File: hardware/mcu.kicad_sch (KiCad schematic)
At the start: 35 parts, among them J10 Conn_01x06, J11 Conn_01x02, J7 TC2030, J8 Conn_01x04, J9 Conn_01x06, U3 AT25SF081-SSHD-B, U4 MCP9808, U5 STM32L552CEU6, Y1 ECS-160-9-37-CKM-TR3, Y2 ABS05-32.768KHZ-9-T

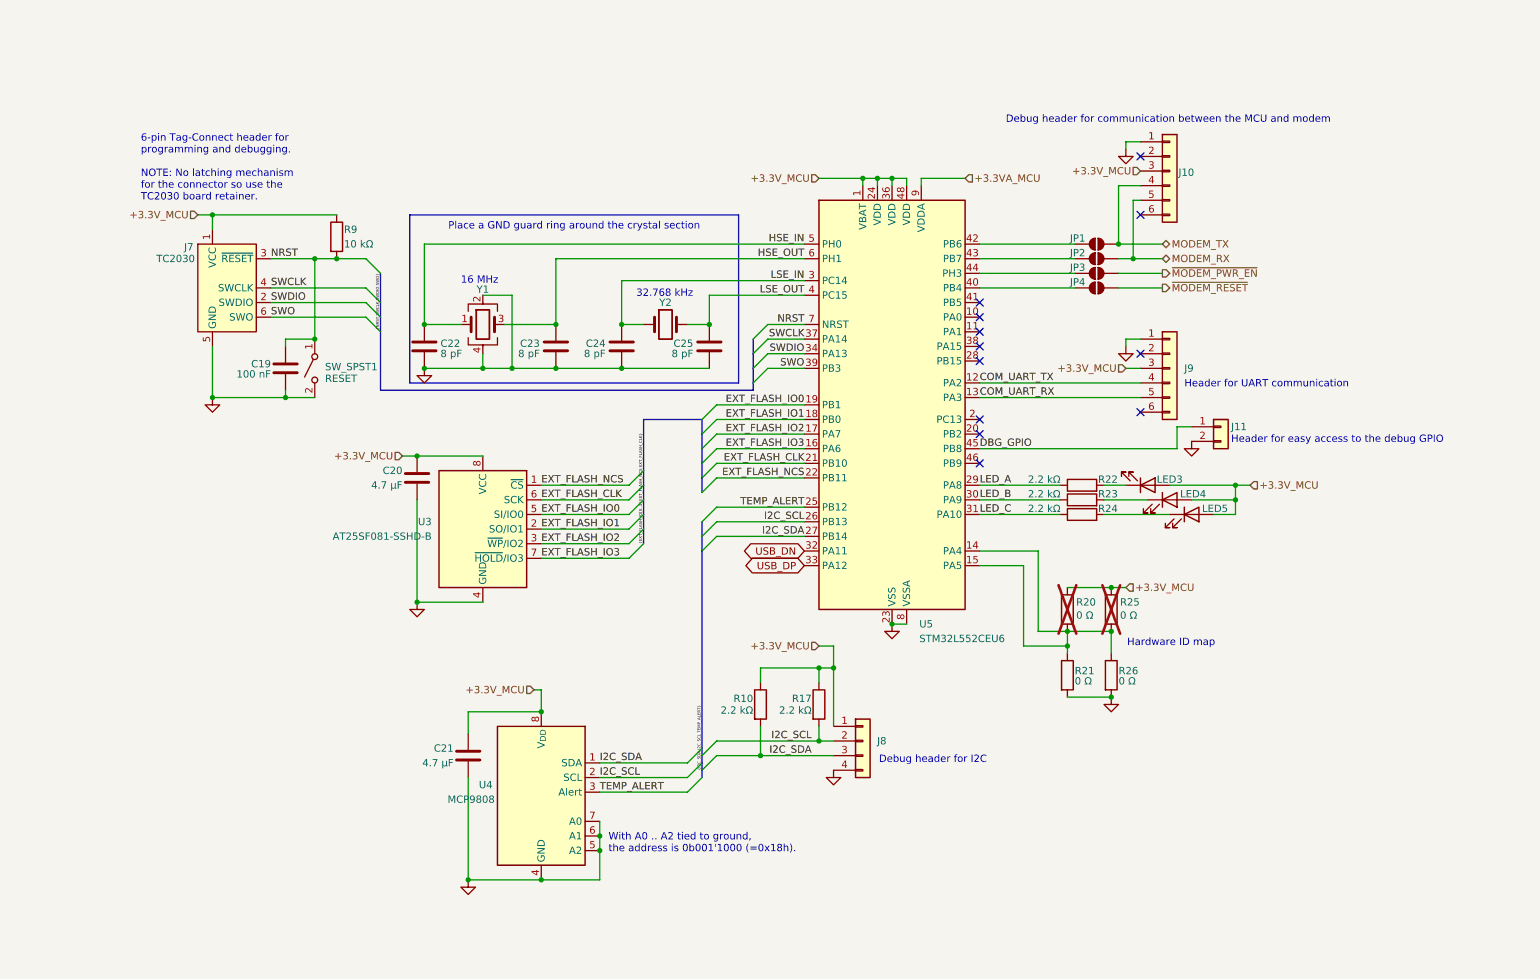
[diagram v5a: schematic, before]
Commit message: HW: Make sections more compact
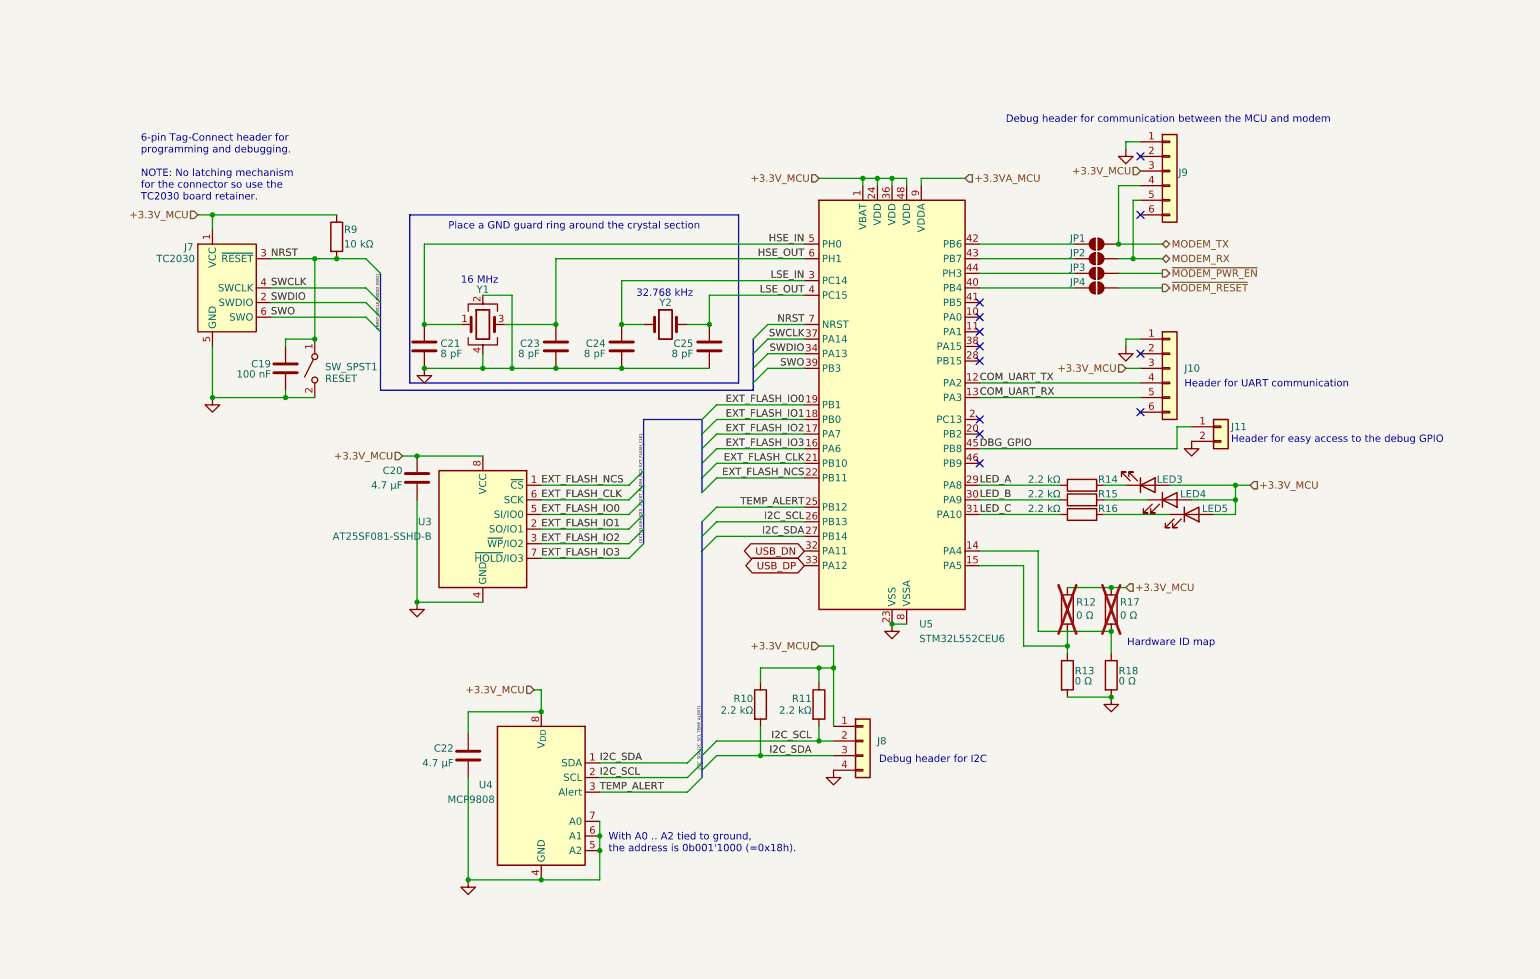
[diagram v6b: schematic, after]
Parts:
- renumbered C22 to C21, C21 to C22, J9 to J10, J10 to J9, R17 to R11, R20 to R12, R21 to R13, R22 to R14, R23 to R15, R24 to R16, R25 to R17, R26 to R18
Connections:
- net at R12.2, R13.1, U5.15 (PA5): no longer R17.2, R18.1, U5.14 (PA4)
- new net: R17.2, R18.1, U5.14 (PA4)
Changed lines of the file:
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@@
 	)
 	(junction
-		(at 195.58 130.81)
-		(diameter 0)
-		(color 0 0 0 0)
-	)
-	(junction
 		(at 104.14 173.99)
 		(diameter 0)
@@
 	)
 	(junction
+		(at 203.2 130.81)
+		(diameter 0)
+		(color 0 0 0 0)
+	)
+	(junction
 		(at 106.68 77.47)
 		(diameter 0)
@@
 	)
 	(junction
-		(at 203.2 130.81)
-		(diameter 0)
-		(color 0 0 0 0)
-	)
-	(junction
 		(at 152.4 137.16)
 		(diameter 0)
@@
 	(wire
 		(pts
+			(xy 190.5 130.81) (xy 203.2 130.81)
+		)
+		(stroke
+			(width 0)
+			(type default)
+		)
+	)
+	(wire
+		(pts
 			(xy 46.99 58.42) (xy 46.99 60.96)
 		)
@@
 	(wire
 		(pts
-			(xy 118.11 85.09) (xy 133.35 85.09)
+			(xy 203.2 130.81) (xy 203.2 134.62)
 		)
 		(stroke
@@
 		)
 	)
-	(bus
+	(wire
 		(pts
-			(xy 132.08 101.6) (xy 132.08 104.14)
+			(xy 118.11 85.09) (xy 133.35 85.09)
 		)
 		(stroke
@@
 		)
 	)
-	(wire
+	(bus
 		(pts
-			(xy 203.2 130.81) (xy 195.58 130.81)
+			(xy 132.08 101.6) (xy 132.08 104.14)
 		)
 		(stroke
@@
 	(wire
 		(pts
-			(xy 195.58 130.81) (xy 190.5 130.81)
-		)
-		(stroke
-			(width 0)
-			(type default)
-		)
-	)
-	(wire
-		(pts
 			(xy 59.69 80.01) (xy 64.77 80.01)
 		)
@@
 	(wire
 		(pts
-			(xy 203.2 130.81) (xy 203.2 134.62)
-		)
-		(stroke
-			(width 0)
-			(type default)
-		)
-	)
-	(wire
-		(pts
 			(xy 162.56 52.07) (xy 162.56 53.34)
 		)
@@
 		(on_board yes)
 		(dnp yes)
-		(property "Reference" "R20"
+		(property "Reference" "R12"
 			(at 197.104 125.73 0)
 			(effects
@@
 			(project "iida_devkit"
 				(path "/b12a6e25-97fb-4aba-bc96-af8db389bb9a/6dd8d741-3080-458c-a4f5-a05a3905bb8a"
-					(reference "R20")
+					(reference "R12")
 					(unit 1)
 				)
@@
 		(dnp no)
 		(fields_autoplaced yes)
-		(property "Reference" "#PWR017"
+		(property "Reference" "#PWR016"
 			(at 205.74 53.34 0)
 			(effects
@@
 			(project "iida_devkit"
 				(path "/b12a6e25-97fb-4aba-bc96-af8db389bb9a/6dd8d741-3080-458c-a4f5-a05a3905bb8a"
-					(reference "#PWR017")
+					(reference "#PWR016")
 					(unit 1)
 				)
@@
 		(dnp no)
 		(fields_autoplaced yes)
-		(property "Reference" "J9"
+		(property "Reference" "J10"
 			(at 215.9 85.0899 0)
 			(effects
@@
 			(project "iida_devkit"
 				(path "/b12a6e25-97fb-4aba-bc96-af8db389bb9a/6dd8d741-3080-458c-a4f5-a05a3905bb8a"
-					(reference "J9")
+					(reference "J10")
 					(unit 1)
 				)
@@
 		(on_board yes)
 		(dnp no)
-		(property "Reference" "C21"
+		(property "Reference" "C22"
 			(at 88.9 151.13 0)
 			(effects
@@
 			(project "iida_devkit"
 				(path "/b12a6e25-97fb-4aba-bc96-af8db389bb9a/6dd8d741-3080-458c-a4f5-a05a3905bb8a"
-					(reference "C21")
+					(reference "C22")
 					(unit 1)
 				)
@@
 		(on_board yes)
 		(dnp no)
-		(property "Reference" "J10"
+		(property "Reference" "J9"
 			(at 214.884 51.054 0)
 			(effects
@@
 			(project "iida_devkit"
 				(path "/b12a6e25-97fb-4aba-bc96-af8db389bb9a/6dd8d741-3080-458c-a4f5-a05a3905bb8a"
-					(reference "J10")
+					(reference "J9")
 					(unit 1)
 				)
@@
 		(on_board yes)
 		(dnp no)
-		(property "Reference" "R23"
+		(property "Reference" "R15"
 			(at 200.914 106.934 90)
 			(effects
@@
 			(project "iida_devkit"
 				(path "/b12a6e25-97fb-4aba-bc96-af8db389bb9a/6dd8d741-3080-458c-a4f5-a05a3905bb8a"
-					(reference "R23")
+					(reference "R15")
 					(unit 1)
 				)
@@
 		(dnp no)
 		(fields_autoplaced yes)
-		(property "Reference" "#PWR016"
+		(property "Reference" "#PWR017"
 			(at 205.74 87.63 0)
 			(effects
@@
 			(project "iida_devkit"
 				(path "/b12a6e25-97fb-4aba-bc96-af8db389bb9a/6dd8d741-3080-458c-a4f5-a05a3905bb8a"
-					(reference "#PWR016")
+					(reference "#PWR017")
 					(unit 1)
 				)
@@
 		(on_board yes)
 		(dnp no)
-		(property "Reference" "R22"
+		(property "Reference" "R14"
 			(at 200.914 104.394 90)
 			(effects
@@
 			(project "iida_devkit"
 				(path "/b12a6e25-97fb-4aba-bc96-af8db389bb9a/6dd8d741-3080-458c-a4f5-a05a3905bb8a"
-					(reference "R22")
+					(reference "R14")
 					(unit 1)
 				)
@@
 		(on_board yes)
 		(dnp no)
-		(property "Reference" "R17"
+		(property "Reference" "R11"
 			(at 151.13 142.494 0)
 			(effects
@@
 			(project "iida_devkit"
 				(path "/b12a6e25-97fb-4aba-bc96-af8db389bb9a/6dd8d741-3080-458c-a4f5-a05a3905bb8a"
-					(reference "R17")
+					(reference "R11")
 					(unit 1)
 				)
@@
 		(on_board yes)
 		(dnp no)
-		(property "Reference" "R26"
+		(property "Reference" "R18"
 			(at 204.47 137.668 0)
 			(effects
@@
 			(project "iida_devkit"
 				(path "/b12a6e25-97fb-4aba-bc96-af8db389bb9a/6dd8d741-3080-458c-a4f5-a05a3905bb8a"
-					(reference "R26")
+					(reference "R18")
 					(unit 1)
 				)
@@
 		(on_board yes)
 		(dnp yes)
-		(property "Reference" "R25"
+		(property "Reference" "R17"
 			(at 204.724 125.73 0)
 			(effects
@@
 			(project "iida_devkit"
 				(path "/b12a6e25-97fb-4aba-bc96-af8db389bb9a/6dd8d741-3080-458c-a4f5-a05a3905bb8a"
-					(reference "R25")
+					(reference "R17")
 					(unit 1)
 				)
@@
 		(on_board yes)
 		(dnp no)
-		(property "Reference" "C22"
+		(property "Reference" "C21"
 			(at 86.614 80.772 0)
 			(effects
@@
 			(project "iida_devkit"
 				(path "/b12a6e25-97fb-4aba-bc96-af8db389bb9a/6dd8d741-3080-458c-a4f5-a05a3905bb8a"
-					(reference "C22")
+					(reference "C21")
 					(unit 1)
 				)
@@
 		(on_board yes)
 		(dnp no)
-		(property "Reference" "R24"
+		(property "Reference" "R16"
 			(at 200.914 109.474 90)
 			(effects
@@
 			(project "iida_devkit"
 				(path "/b12a6e25-97fb-4aba-bc96-af8db389bb9a/6dd8d741-3080-458c-a4f5-a05a3905bb8a"
-					(reference "R24")
+					(reference "R16")
 					(unit 1)
 				)
@@
 		(dnp no)
 		(fields_autoplaced yes)
-		(property "Reference" "#PWR012"
+		(property "Reference" "#PWR011"
 			(at 83.82 91.44 0)
 			(effects
@@
 			(project "iida_devkit"
 				(path "/b12a6e25-97fb-4aba-bc96-af8db389bb9a/6dd8d741-3080-458c-a4f5-a05a3905bb8a"
-					(reference "#PWR012")
+					(reference "#PWR011")
 					(unit 1)
 				)
@@
 		(dnp no)
 		(fields_autoplaced yes)
-		(property "Reference" "#PWR011"
+		(property "Reference" "#PWR012"
 			(at 91.44 180.34 0)
 			(effects
@@
 			(project "iida_devkit"
 				(path "/b12a6e25-97fb-4aba-bc96-af8db389bb9a/6dd8d741-3080-458c-a4f5-a05a3905bb8a"
-					(reference "#PWR011")
+					(reference "#PWR012")
 					(unit 1)
 				)
@@
 		(on_board yes)
 		(dnp no)
-		(property "Reference" "R21"
+		(property "Reference" "R13"
 			(at 196.85 137.668 0)
 			(effects
@@
 			(project "iida_devkit"
 				(path "/b12a6e25-97fb-4aba-bc96-af8db389bb9a/6dd8d741-3080-458c-a4f5-a05a3905bb8a"
-					(reference "R21")
+					(reference "R13")
 					(unit 1)
 				)

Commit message: HW: Rework power section
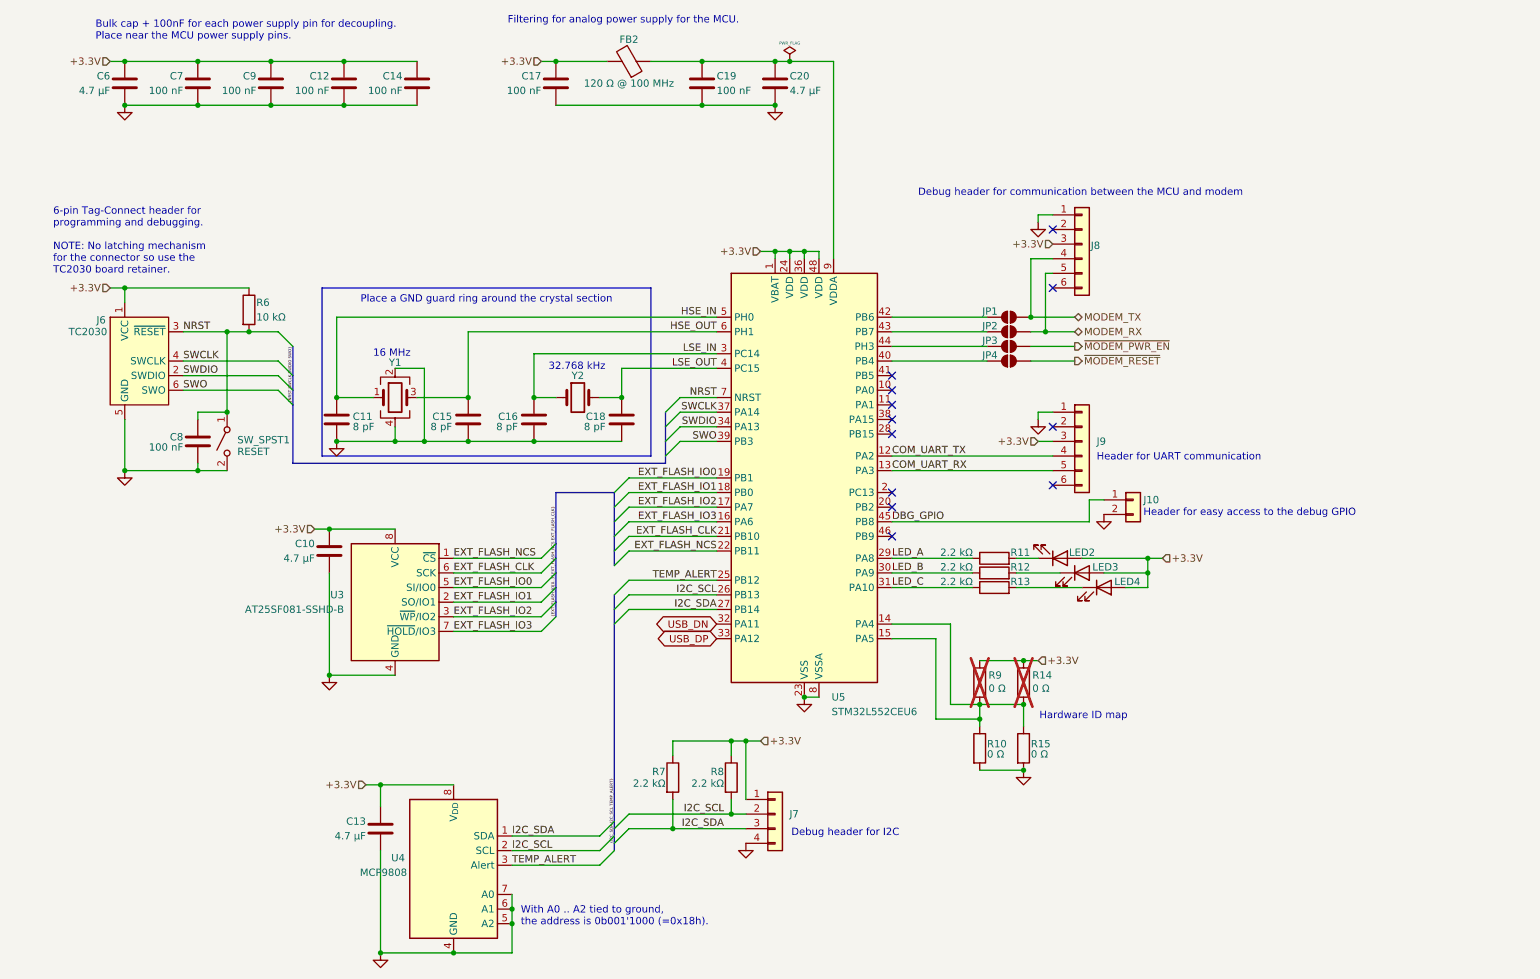
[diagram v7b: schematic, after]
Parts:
- added C12, C14, C17, C19, C7, C9: 100 nF, perfect_footprints:0402_1005_perfect, symbol Device:C
- added C20, C6: 4.7 µF, Capacitor_SMD:C_0603_1608Metric, symbol Device:C
- added FB2: 120 Ω @ 100 MHz, Resistor_SMD:R_0603_1608Metric, symbol Device:FerriteBead
- renumbered C20 to C10, C21 to C11, C22 to C13, C23 to C15, C24 to C16, C25 to C18, C19 to C8, J11 to J10, J7 to J6, J8 to J7, J9 to J8, J10 to J9, LED3 to LED2, LED4 to LED3, LED5 to LED4, R13 to R10, R14 to R11, R15 to R12, R16 to R13, R17 to R14, R18 to R15, R9 to R6, R10 to R7, R11 to R8, R12 to R9
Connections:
- net GND: now also C12.2, C14.2, C17.2, C19.2, C20.2, C6.2, C7.2, C9.2
- net at R10.1, R9.2, U5.15 (PA5): now also R14.2, R15.1, U5.14 (PA4)
- net +3.3VA_MCU: no longer names the net of U5.9 (VDDA)
- net +3.3VA_MCU: now also C19.1, C20.1, FB2.1
- net +3.3V_MCU renamed +3.3V
- net +3.3V: now also C12.1, C14.1, C17.1, C6.1, C7.1, C9.1, FB2.2
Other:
- note added: "Bulk cap + 100nF for each power supply pin for decoupling. Place near the MCU power supply pins."
- note added: "Filtering for analog power supply for the MCU."
- moved on the sheet: C10, C11, C13, C15, C16, C18, C8, J10, J6, J7, J8, J9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

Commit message: HW: Initial layout and routing done
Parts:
- U3: value AT25SF081-SSHD-B -> AT25SF081B-SSHD-B
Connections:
- net at R10.1, R9.2, U5.15 (PA5): no longer R14.2, R15.1, U5.14 (PA4)
- new net: R14.2, R15.1, U5.14 (PA4)
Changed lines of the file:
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@@
 	(title_block
 		(title "Iida devkit")
-		(date "2024-09-08")
+		(date "2024-09-10")
 		(rev "v4.0.0")
 	)
@@
 	)
 	(junction
-		(at 180.34 143.51)
-		(diameter 0)
-		(color 0 0 0 0)
-	)
-	(junction
 		(at 31.75 39.37)
 		(diameter 0)
@@
 	(wire
 		(pts
-			(xy 180.34 143.51) (xy 187.96 143.51)
+			(xy 175.26 143.51) (xy 187.96 143.51)
 		)
 		(stroke
@@
 	(wire
 		(pts
-			(xy 175.26 143.51) (xy 180.34 143.51)
-		)
-		(stroke
-			(width 0)
-			(type default)
-		)
-	)
-	(wire
-		(pts
 			(xy 31.75 71.12) (xy 31.75 73.66)
 		)
@@
 			)
 		)
-		(property "Value" "AT25SF081-SSHD-B"
+		(property "Value" "AT25SF081B-SSHD-B"
 			(at 69.85 126.9999 0)
 			(effects
